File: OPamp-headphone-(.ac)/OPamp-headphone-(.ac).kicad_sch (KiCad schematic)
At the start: 9 parts, among them U1 LM741

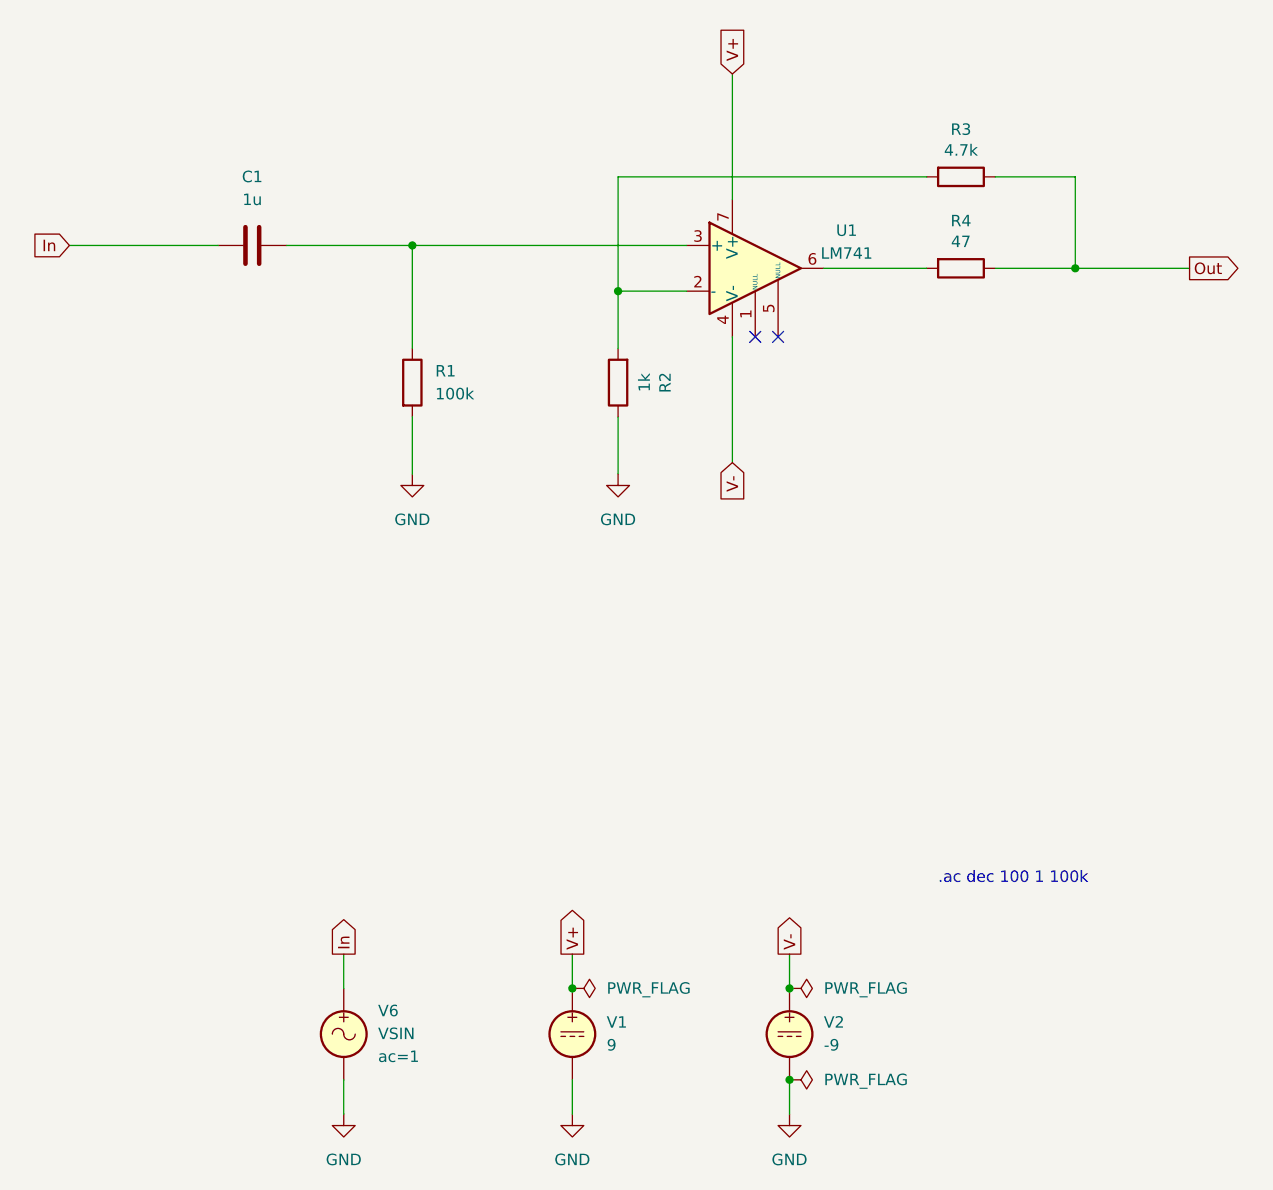
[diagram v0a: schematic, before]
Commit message: Updated all schematics and prepared for KiCad 8.0
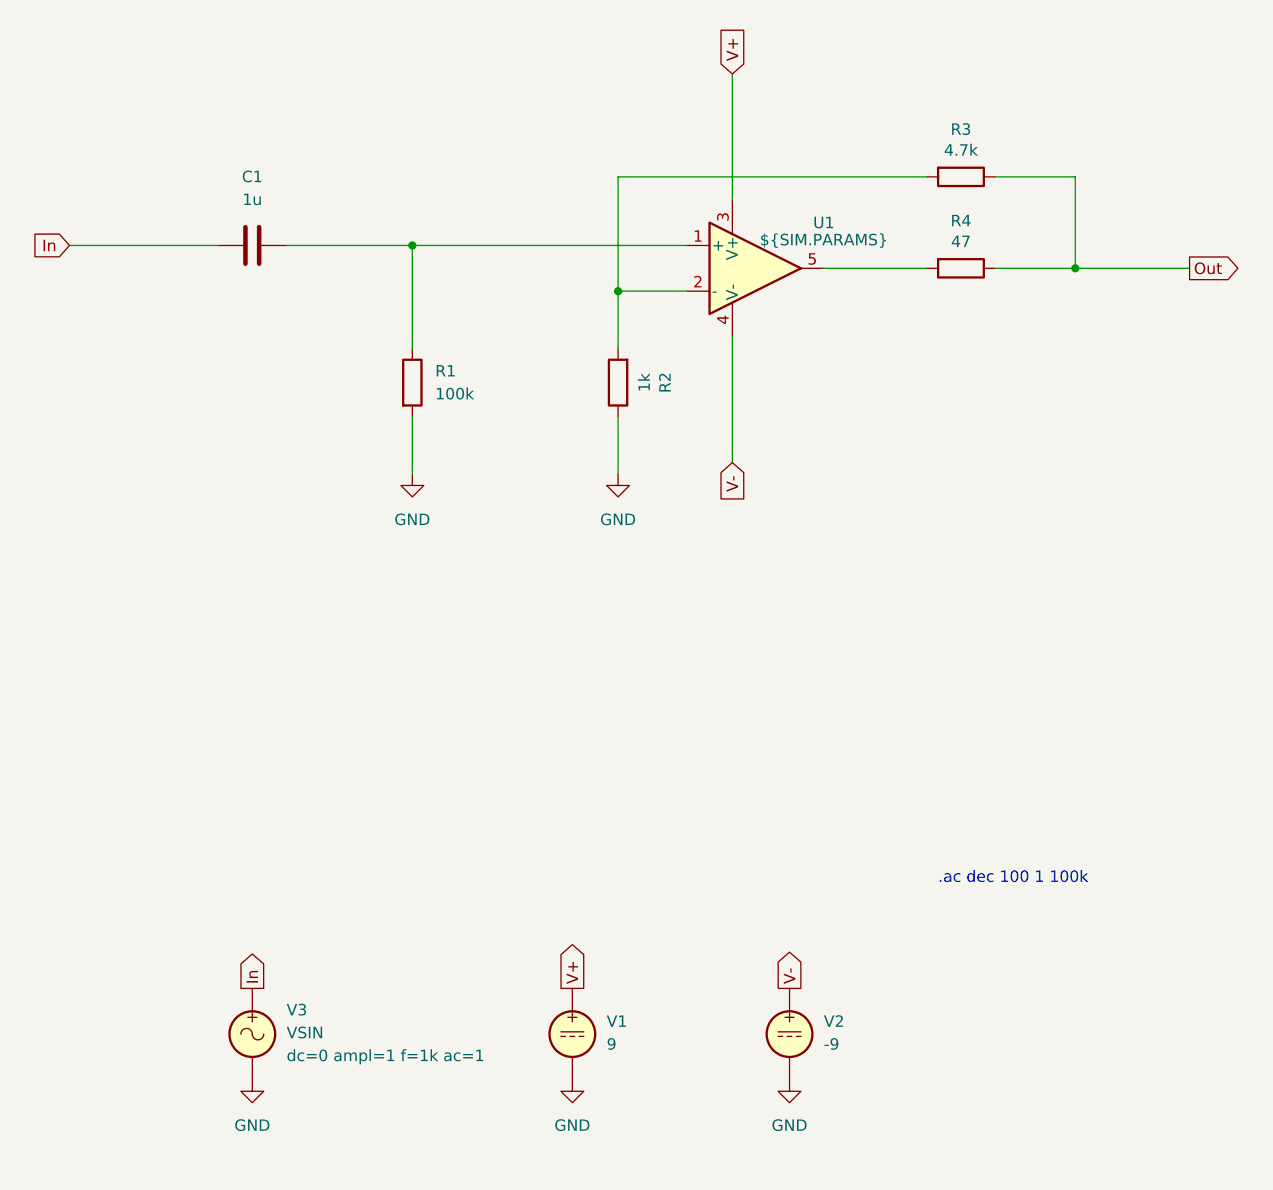
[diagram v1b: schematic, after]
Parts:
- removed U1: LM741, symbol Amplifier_Operational:LM741
- removed V6: VSIN, symbol Simulation_SPICE:VSIN
- added U1: ${SIM.PARAMS}, symbol Simulation_SPICE:OPAMP
- added V3: VSIN, symbol Simulation_SPICE:VSIN
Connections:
- net GND: now also V3.2
- net In: now also V3.1
- net V+: now also U1.3 (V+)
- net V-: now also U1.4 (V-)
- net at R2.2, R3.2: now also U1.2 (-)
- net at C1.2, R1.1: now also U1.1 (+)
- net at R4.2: now also U1.5
- no-connect marks 2 -> 0
